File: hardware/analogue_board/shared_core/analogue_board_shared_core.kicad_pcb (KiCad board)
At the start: 4 copper layers, 49.6 x 103 mm, 372 parts, among them J1001 TRS MIDI holes, J101 Spare GPIO, MIDI links, RUN, J201 Eurorack power 2x5 shrouded, J303 Codec RST, J310 Holes, left top, J311 Holes, left bottom, J312 Holes, right top, J313 Holes, right middle, J410 Holes, left top, J411 Holes, left bottom, J412 Holes, left top, J413 Holes, right top, J414 Holes, right middle, J603 Gate expansion: QH', SRCLK, R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, J610 Holes, left top, J611 Holes, left bottom, J612 Holes, left top, J613 Holes, left bottom, J614 Holes, right top, J615 Holes, right middle, J703 I2C holes for a wired display, J704 WS2812 chain holes, J710 Holes, left top, J711 Holes, left bottom, J712 Holes, left top, J713 Holes, left bottom, J714 Holes, right top, J715 Holes, right middle, J810 Holes, left top, J811 Holes, left bottom, J812 Holes, right top, J813 Holes, right middle, J901 Edge strip, left, J902 Edge strip, right, Q201 AO3401A, U1001 SN74AHCT1G125DBVR, U1002 H11L1SR2M, U201 TPS54308DDCR, U202 L78M05ABDT-TR, U203 XC6206P332MR-G, U204 XC6206P332MR-G, U301 PCM3060PWR, U302 TL074HIDR, U401 ADS8688IDBTR, U402 DG412DQ-T1-E3, U403 DG412DQ-T1-E3, U501 DAC8568IAPWR, U502 TL074HIDR, U504 TL074HIDR, U601 MCP3208-CI/SL, U602 74HCT595PW, U701 TCA9555PWR, U702 M24C64-RMN6TP, U703 SN74AHCT1G125DBVR, U801 LM393DR2G, U802 LM393DR2G

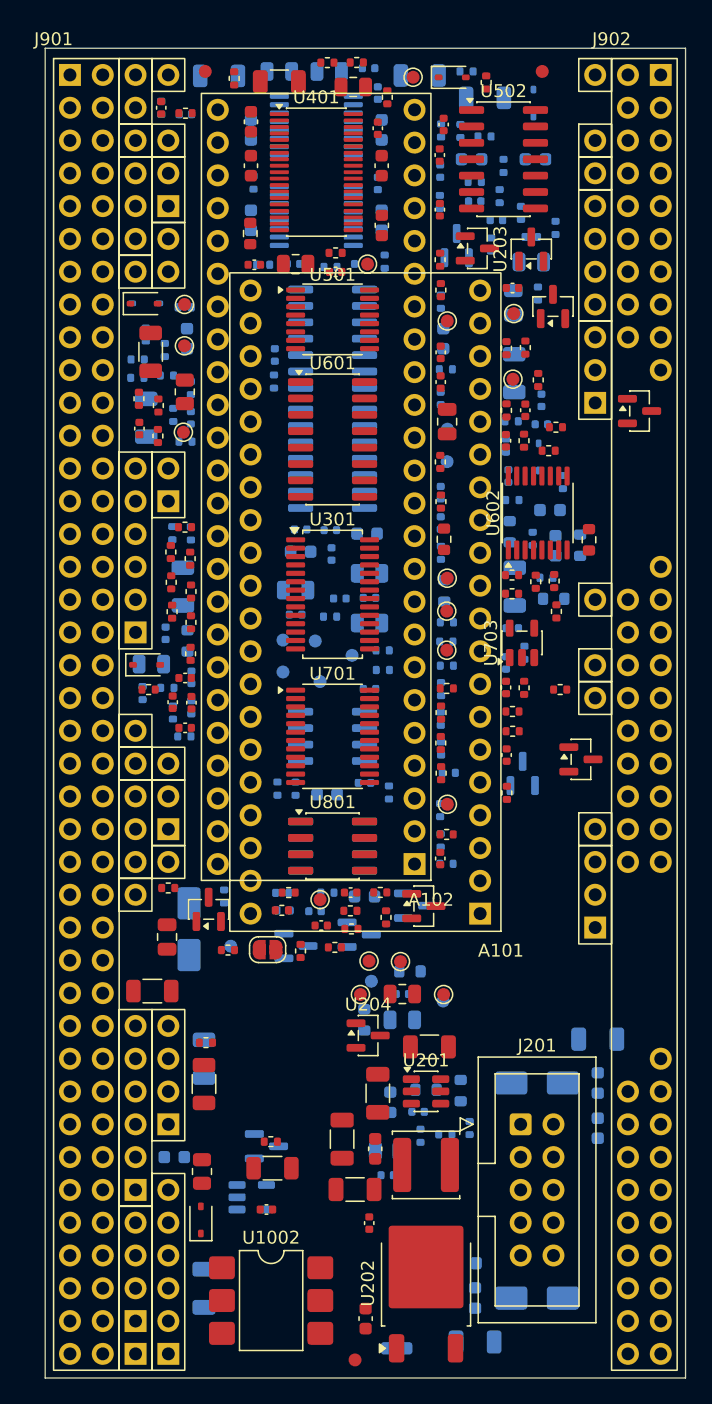
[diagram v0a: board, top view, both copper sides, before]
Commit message: Analogue board: the Teensy core board routes completely
teensy_core_midi (Teensy 4.1 alone, the shared core feature set with TRS MIDI) routes with no
unconnected item and no copper fault in KiCad's DRC. Its routed board is kept in
teensy_core_midi/routed_trial/.

The route is scripted end to end:
- autoroute.py --ground-vias gives every surface-mount ground pad its own via to the plane
  before routing (Freerouting alone joined 207 ground pads through 38 vias and 567 mm of track)
- autoroute.py --decoupling wires each decoupling capacitor to the pin it serves first
- Freerouting stages 1 and 2 (--stages=2); stage 3 was dropped
- finish.py: via drills, narrow tracks, copper faults taken up, leftovers routed on its own
  grid router, then rip-up and reroute; dead ends removed; ground stitched
- fab.py: Gerbers, drill, JLC BOM and CPL

Placement: the DG412s turn 90 degrees across the chip above them; the auto-placer charges for
each module header row between a part and its pins; FB301 sits by the codec pin it feeds. On
the Teensy board, David's review moved the 595 into the left void, the LDO out from under the
module and five right-column holes into the right strip's empty positions 11-15.

Also new: pico_core_midi (Pico board, module 8 mm lower), still finishing. 0.1 mm rules were
tried on shared_core and routed worse; it stays at 0.127 mm.

Co-Authored-By: Claude Opus 5.5 <noreply@anthropic.com>
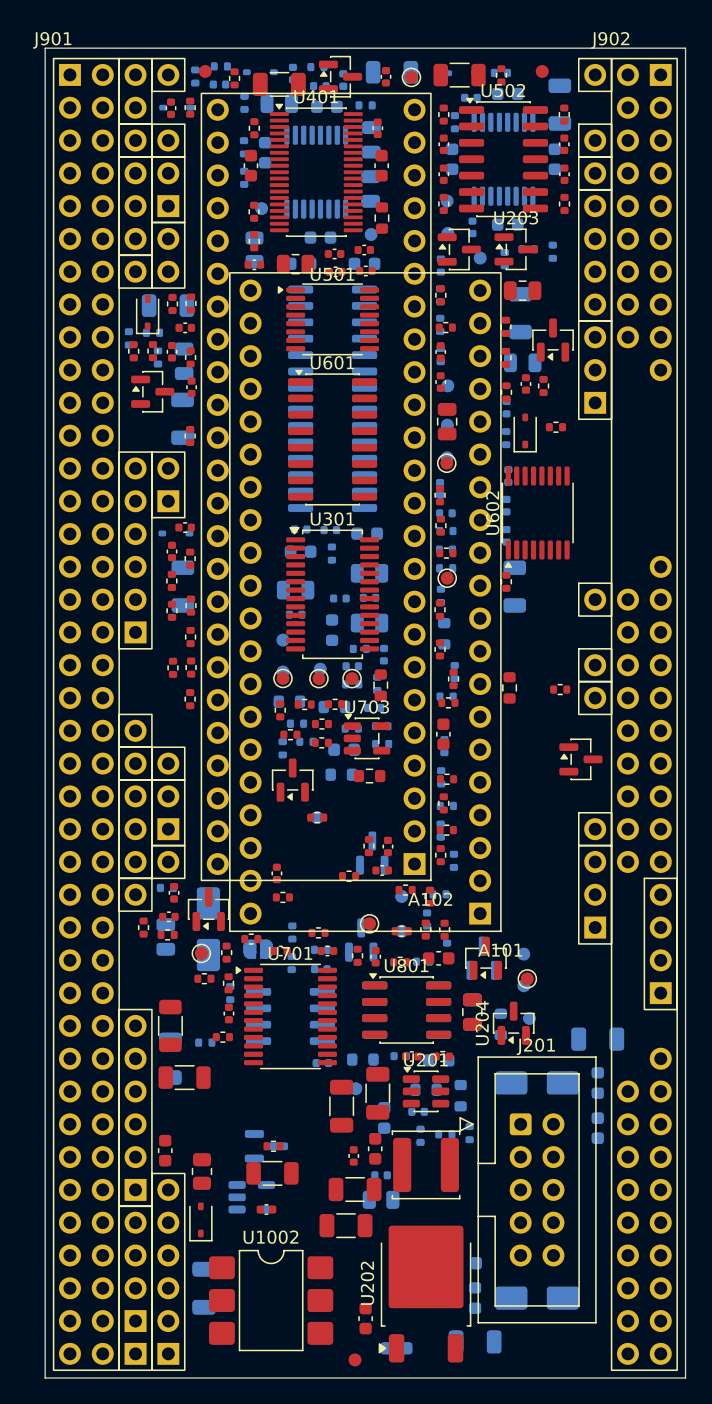
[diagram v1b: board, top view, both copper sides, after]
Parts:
- C1003, C219, C318, C412, C413, C507, C509, C510, C604, C605, C606, C608, C701, C706, C708, C801, D302, D406, D602, D802, R211, R303, R311, R314, R327, R401, R410, R413, R415, R427, R505, R507, R509, R511, R512, R603, R605, R606, R610, R618, R701, R703, R705, R707, R710, R720, R721, R802, R806, R818, TP201, TP209, TP302, TP604: moved to F.Cu
- C222, C404, C406, C410, C414, C610, C710, D401, D403, D801, FB301, JP201, R1001, R1002, R212, R302, R405, R408, R411, R421, R422, R501, R601, R614, R716, R718, R719, R722, TP202, TP203, TP207, TP208, TP305, TP401, TP402, TP403, TP404, TP605, TP702, TP703: moved to B.Cu
- moved J703 39.5 mm to (77.7, 95.6)
- moved R421 32.3 mm to (38.3, 52.0), turned to 0 degrees
- moved D601 31.7 mm to (38.3, 56.6), turned to 0 degrees
- moved FB301 31.6 mm to (52.2, 75.1)
- moved R423 30.7 mm to (49.5, 82.3), turned to 0 degrees
- moved D405 29.8 mm to (37.9, 50.5), turned to 90 degrees
- moved R301 29.7 mm to (49.0, 83.2)
- moved R413 29.4 mm to (38.3, 53.5)
- moved R427 28.7 mm to (48.2, 81.3), turned to 90 degrees
- moved R318 28.3 mm to (50.2, 83.7), turned to 0 degrees
- moved R503 27.3 mm to (41.6, 32.2)
- moved R419 26.9 mm to (60.6, 73.5)
- moved R606 26.2 mm to (36.9, 53.5), turned to 90 degrees
- moved R320 25.7 mm to (52.9, 86.3), turned to 0 degrees
- moved R415 25.7 mm to (61.1, 69.1)
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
